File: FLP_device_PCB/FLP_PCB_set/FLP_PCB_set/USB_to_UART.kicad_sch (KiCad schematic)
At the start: 1 part, among them U14 CH340N

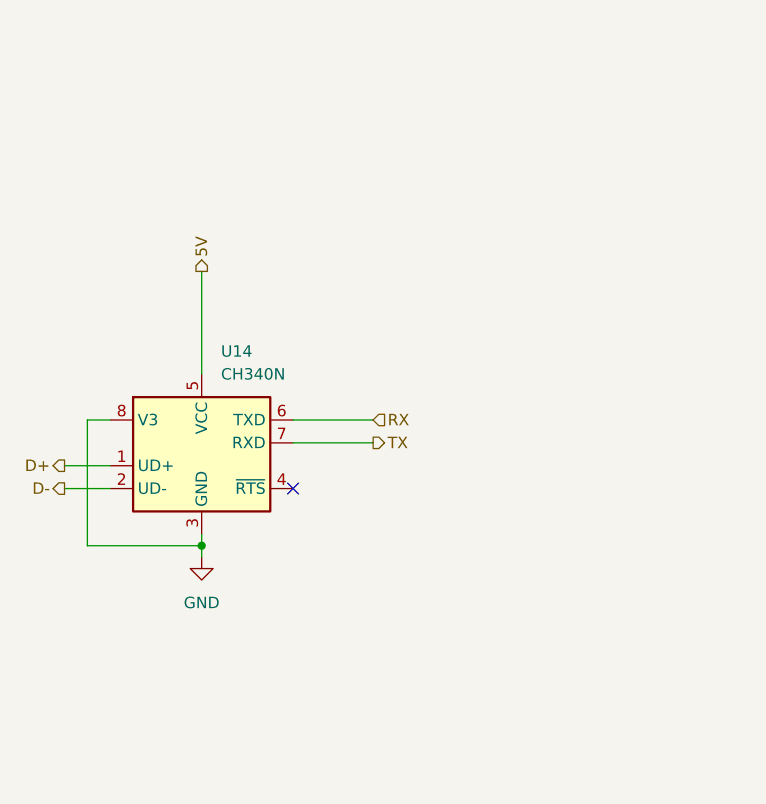
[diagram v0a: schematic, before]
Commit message: PCB fixing end adding description pdf
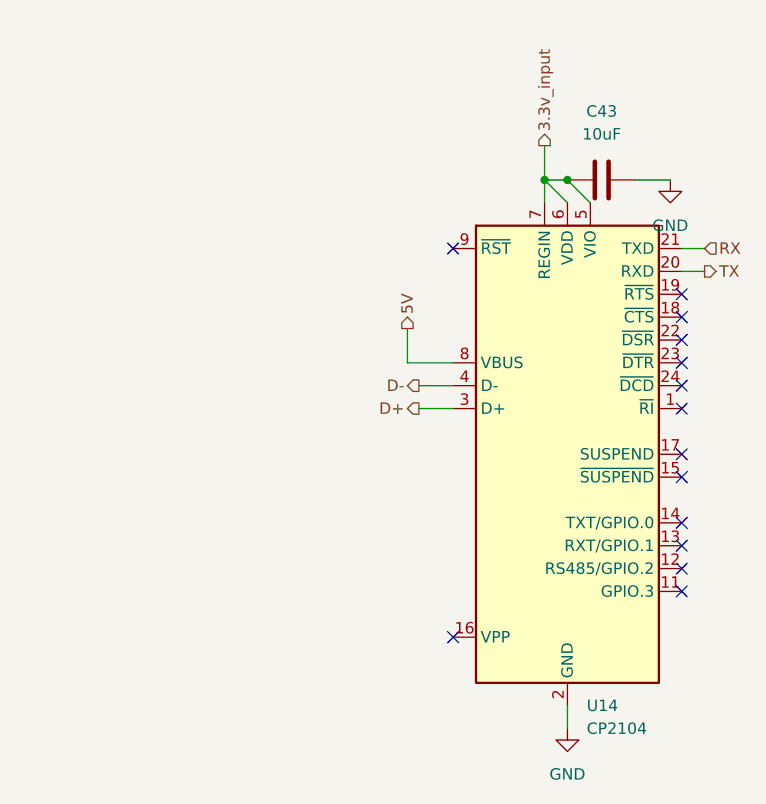
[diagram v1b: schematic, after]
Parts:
- removed U14: CH340N, Package_SO:SOP-8_3.9x4.9mm_P1.27mm, symbol Interface_USB:CH340N
- added C43: 10uF, Capacitor_SMD:C_0805_2012Metric, symbol Device:C
- added U14: CP2104, Package_DFN_QFN:QFN-24-1EP_4x4mm_P0.5mm_EP2.6x2.6mm, symbol Interface_USB:CP2104
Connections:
- net 5V: now also U14.8 (VBUS)
- net D+: now also U14.3 (D+)
- net D-: now also U14.4 (D-)
- net GND: now also C43.2, U14.2 (GND), U14.25 (GND)
- net RX: now also U14.21 (TXD)
- net TX: now also U14.20 (RXD)
- new net 3.3v_input: C43.1, U14.5 (VIO), U14.6 (VDD), U14.7 (REGIN)
- no-connect marks 1 -> 14
